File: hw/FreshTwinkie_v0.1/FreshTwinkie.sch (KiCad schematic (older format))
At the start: 50 parts, among them J1 USB_C_Receptacle, J2 USB_B_Micro, P1 USB_C_Plug, Q1 BSD840NH6327XTSA1, Q2 BSD840NH6327XTSA1, Q3 BSD840NH6327XTSA1, Q4 BSD840NH6327XTSA1, SW1 SW_Push, U1 AD8606ARMZ-REEL, U2 STM32F072CBUx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

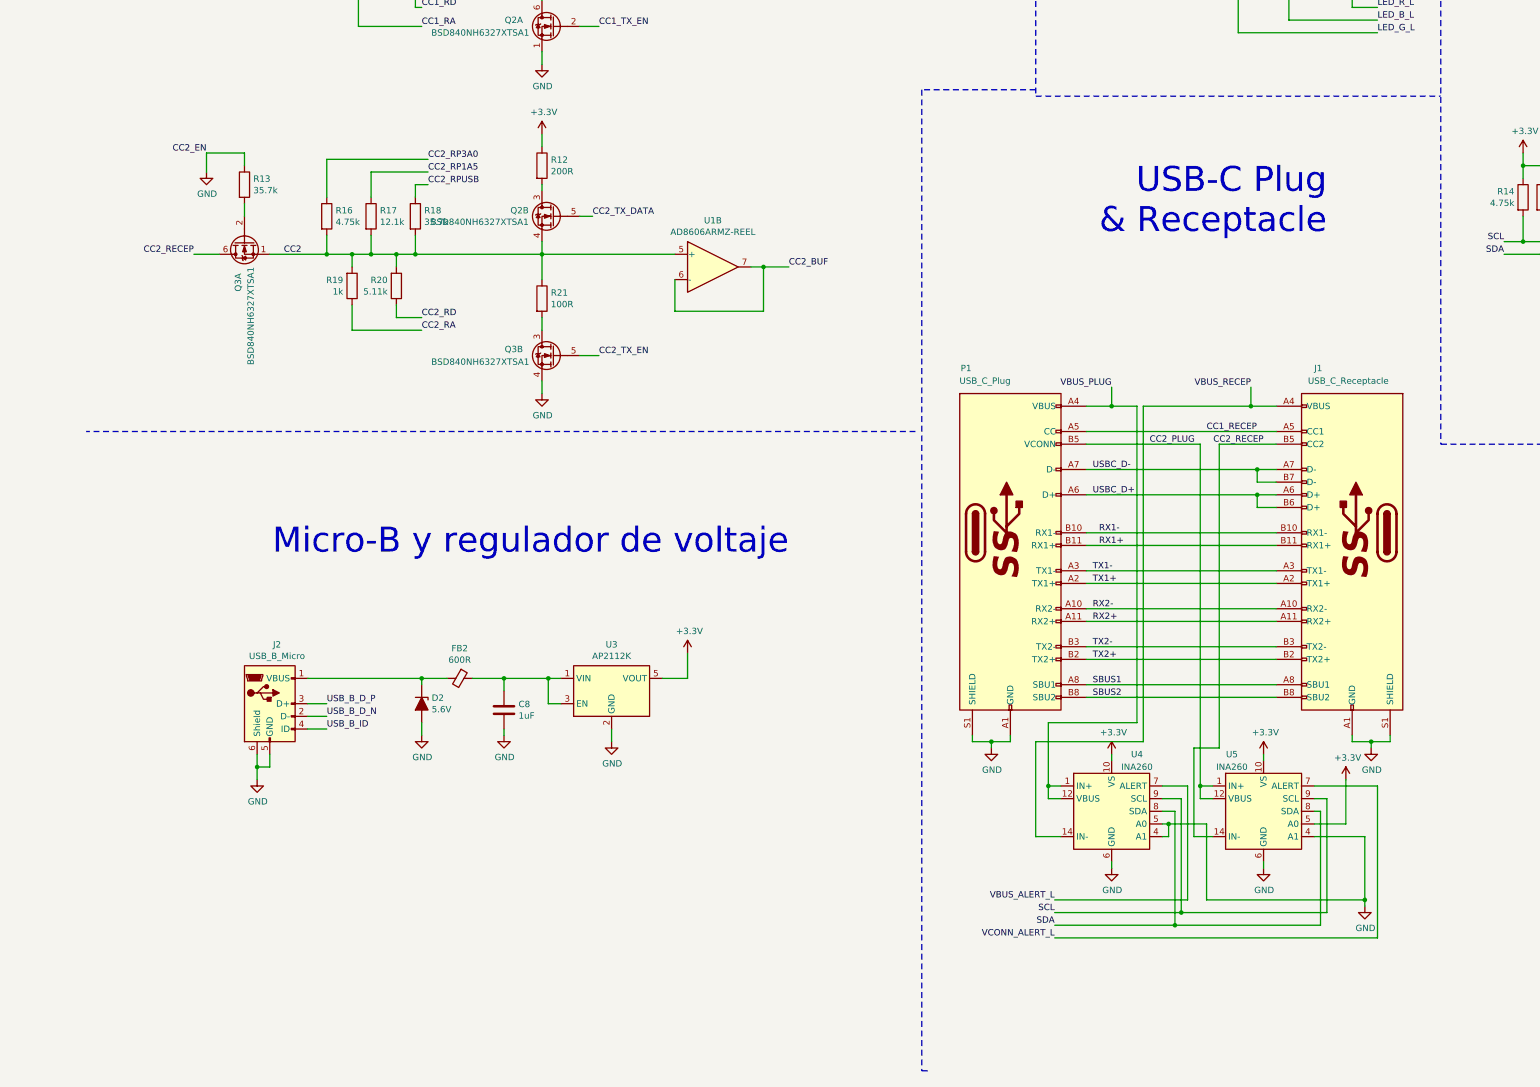
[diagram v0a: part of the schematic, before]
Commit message: switchINA260&RShunt
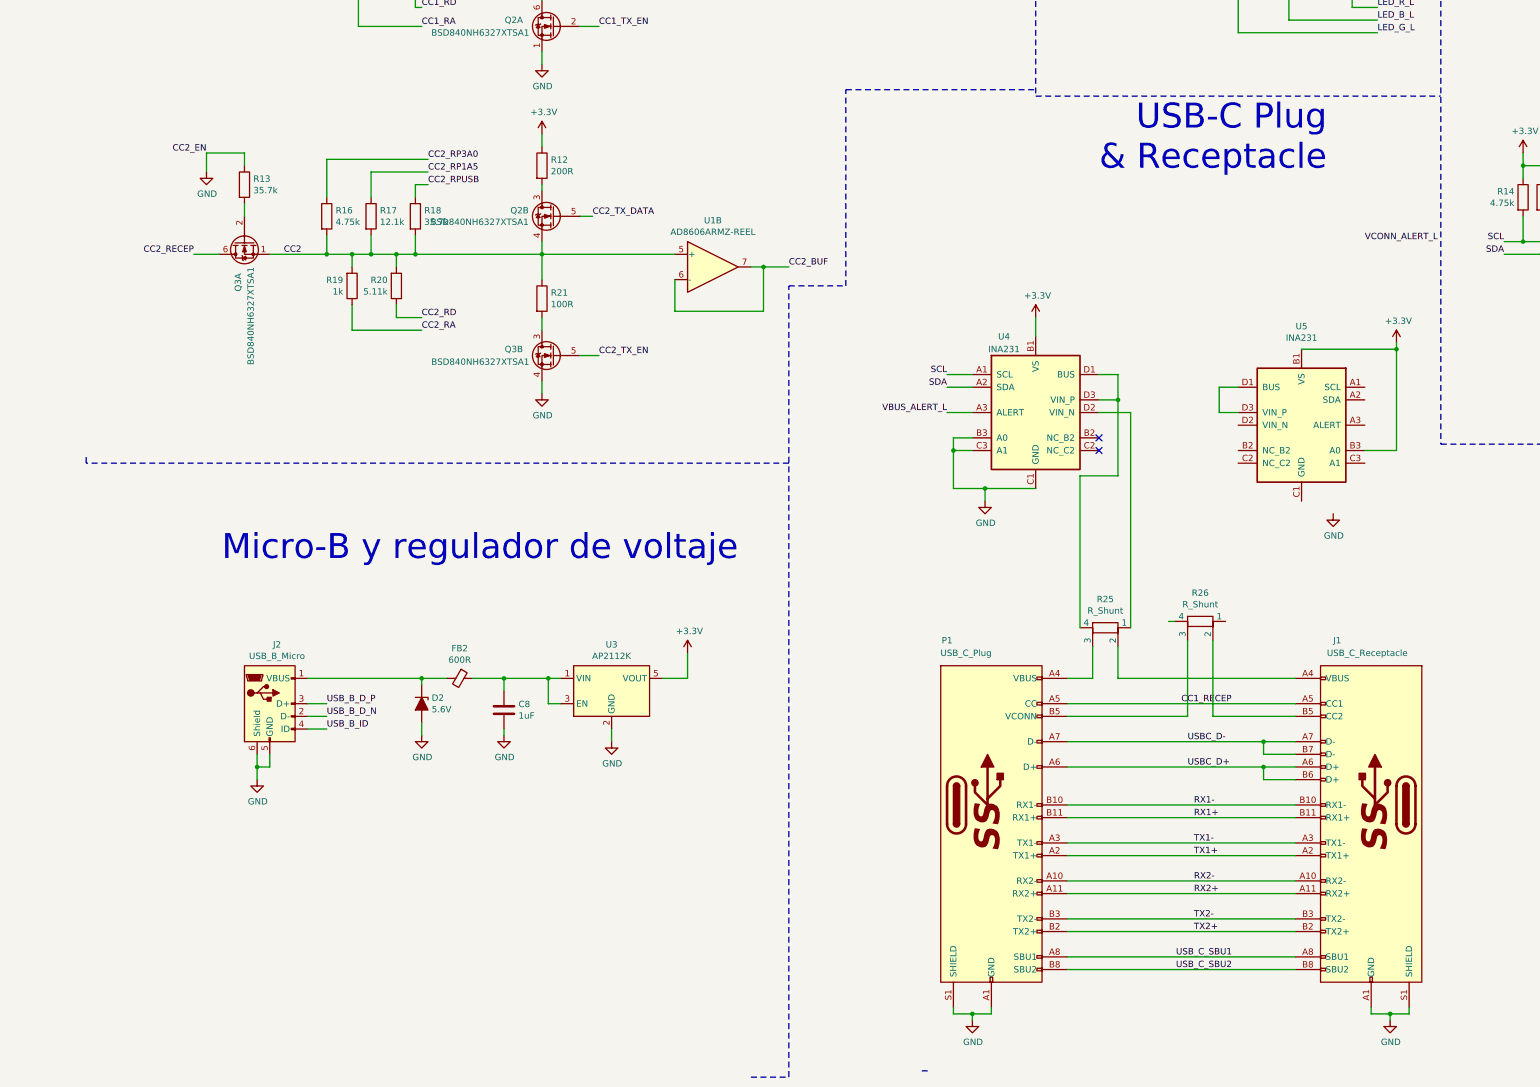
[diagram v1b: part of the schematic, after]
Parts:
- removed U4, U5: INA260, Package_SO:TSSOP-16_4.4x5mm_P0.65mm, symbol Sensor:INA260
- added R25, R26: R_Shunt, symbol Device:R_Shunt
- added U4, U5: INA231, symbol gkl_sensor:INA231
- C1: footprint Capacitor_SMD:C_0805_2012Metric -> Capacitor_SMD:C_0603_1608Metric; Mfg Taiyo Yuden -> Samsung; PN C385902 -> C1705
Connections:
- net +3V3: now also U4.B1 (VS), U5.B1 (VS), U5.B3 (A0)
- net CC2_RECEP: no longer J1.B5 (CC2)
- net GND: now also U4.B3 (A0), U4.C1 (GND), U4.C3 (A1)
- net SCL: now also U4.A1 (SCL)
- net SDA: now also U4.A2 (SDA)
- net VBUS_ALERT_L: now also U4.A3 (ALERT)
- net CC2_PLUG: no longer names the net of P1.B5 (VCONN)
- net CC2_PLUG: now also R26.3
- net SBUS1 renamed USB_C_SBU1
- net SBUS2 renamed USB_C_SBU2
- net VBUS_PLUG: no longer names the net of P1.A4 (VBUS), P1.A9 (VBUS), P1.B4 (VBUS), P1.B9 (VBUS)
- net VBUS_PLUG: now also R25.3
- net VBUS_RECEP: no longer names the net of J1.A4 (VBUS), J1.A9 (VBUS), J1.B4 (VBUS), J1.B9 (VBUS)
- net VBUS_RECEP: now also R25.2
- new net: J1.B5 (CC2), R26.2
- new net: R25.1, U4.D2 (VIN_N)
- new net: R25.4, U4.D1 (BUS), U4.D3 (VIN_P)
- new net: U5.D1 (BUS), U5.D3 (VIN_P)
- no-connect marks 6 -> 8
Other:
- moved on the sheet: J1, P1

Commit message: schChanged
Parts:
- added NT1: Net-Tie_2, NetTie:NetTie-2_SMD_Pad0.5mm, symbol Device:Net-Tie_2
- R25, R26: value R_Shunt -> 0.015R; footprint (none) -> gkl_dipol:4W_R_1206; Mfg (none) -> Vishay; PN (none) -> 71-WSK1206R0150FEA18; Tienda (none) -> Mouser
- U4, U5: footprint (none) -> BGA12N40P3X4_119X159X62N:BGA12N40P3X4_119X159X62N; Mfg (none) -> Texas Instruments; PN (none) -> 595-INA231AIYFFR; Tienda (none) -> Mouser
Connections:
- net CC2_RECEP is gone; now on net USBC_CC2: Q3.6 (D)
- net VCONN_ALERT_L is gone; now on net CC2_ALERT_L: U2.17 (PA7)
- net CC1_RA: now also U2.29 (PA8); no longer U2.45 (PB8)
- net CC1_RD: now also U2.41 (PB5); no longer U2.39 (PB3)
- net CC1_RP1A5: now also U2.37 (PA14); no longer U2.41 (PB5)
- net CC1_RP3A0: no longer U2.3 (PC14)
- net CC1_RPUSB: now also U2.34 (PA13); no longer U2.37 (PA14)
- net CC1_TX_EN: now also U2.19 (PB1); no longer U2.34 (PA13)
- net CC2_RA: now also U2.28 (PB15); no longer U2.29 (PA8)
- net CC2_RD: now also U2.45 (PB8); no longer U2.26 (PB13)
- net CC2_RP1A5: now also U2.3 (PC14); no longer U2.28 (PB15)
- net CC2_RP3A0: now also U2.4 (PC15)
- net CC2_RPUSB: now also U2.18 (PB0); no longer U2.25 (PB12)
- net CC2_TX_EN: now also U2.39 (PB3); no longer U2.2 (PC13)
- net GND: now also R13.2, R2.2, U5.C1 (GND), U5.C3 (A1); no longer R13.1, R2.1, U2.10 (PA0), U2.12 (PA2)
- net LED_G_L: now also U2.22 (PB11); no longer U2.21 (PB10)
- net LED_R_L: now also U2.26 (PB13); no longer U2.22 (PB11)
- net SCL: now also U5.A1 (SCL)
- net SDA: now also U5.A2 (SDA)
- net TX_CLKIN: now also NT1.1
- net TX_CLKOUT: now also NT1.2
- net USBC_CC2: now reaches J1.B5 (CC2), R26.2
- net CC1_EN: now reaches Q1.5 (G)
- net CC1_EN: now also R2.1, U2.10 (PA0); no longer R2.2
- net CC2_EN: now reaches Q3.2 (G)
- net CC2_EN: now also R13.1, U2.12 (PA2); no longer R13.2
- net USBC_VBUS_-: now reaches R25.1, U4.D2 (VIN_N)
- net USBC_VBUS_+: now reaches R25.4, U4.D1 (BUS), U4.D3 (VIN_P)
- net USBC_CC2_-: now reaches R26.1
- net USBC_CC2_-: now also U5.D2 (VIN_N)
- net USBC_CC2_+: now reaches R26.4
- net USBC_CC2_+: now also U5.D1 (BUS), U5.D3 (VIN_P)
- net CC2_ALERT_L: now reaches U5.A3 (ALERT)
- net CC1_RECEP renamed USBC_CC1
- net USB_B_D_N renamed USB_B_D-
- net USB_B_D_P renamed USB_B_D+
- no-connect marks 8 -> 9
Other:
- moved on the sheet: R13, R2

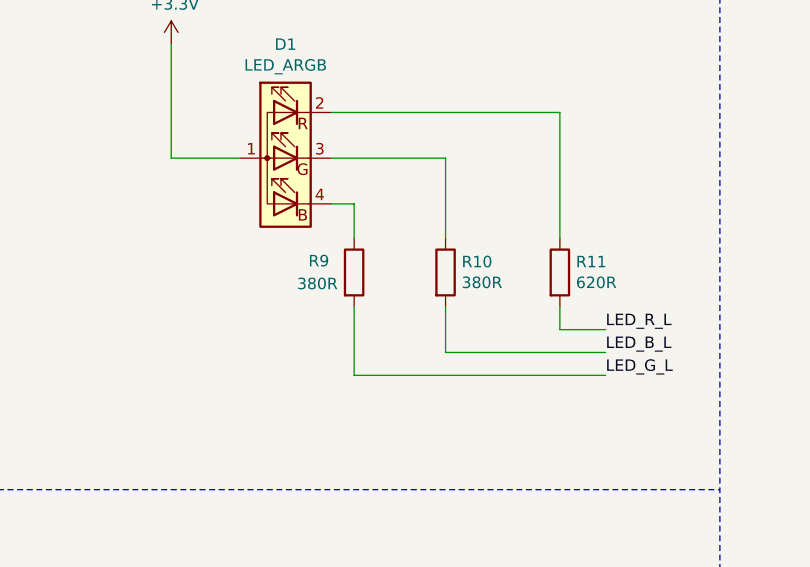
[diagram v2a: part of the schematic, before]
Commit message: 0805into0402components
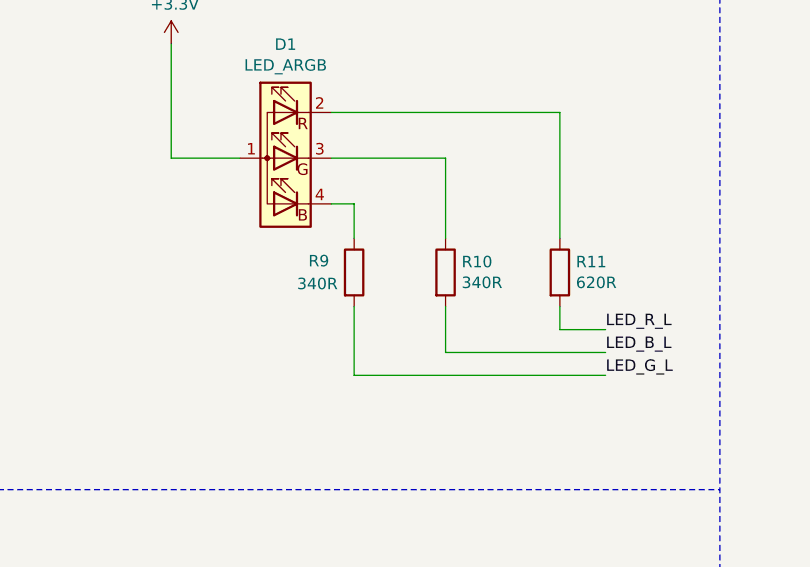
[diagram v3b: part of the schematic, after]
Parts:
- C1: footprint Capacitor_SMD:C_0603_1608Metric -> Capacitor_SMD:C_01005_0402Metric; Mfg Samsung -> Murata; PN C1705 -> C77004
- C2, C3, C7: footprint Capacitor_SMD:C_0805_2012Metric -> Capacitor_SMD:C_01005_0402Metric; Mfg Samsung -> YAGEO; PN 187-CL21F104ZAANNNC -> C60474; Tienda Mouser -> LCSC
- C4: footprint Capacitor_SMD:C_0805_2012Metric -> Capacitor_SMD:C_01005_0402Metric; PN C83170 -> C272878
- C5, C8: footprint Capacitor_SMD:C_0805_2012Metric -> Capacitor_SMD:C_01005_0402Metric; PN 187-CL21B105KOFNFNE -> C307454; Tienda Mouser -> LCSC
- C6: footprint Capacitor_SMD:C_0805_2012Metric -> Capacitor_SMD:C_01005_0402Metric; Mfg Taiyo Yuden -> Murata; PN C385902 -> C77004
- FB1, FB2: footprint Inductor_SMD:L_0805_2012Metric_Pad1.15x1.40mm_HandSolder -> Inductor_SMD:L_01005_0402Metric; PN 81-BLM21A601F -> 81-BLM15BX601SN1D
- R1, R12: footprint Resistor_SMD:R_0805_2012Metric -> Resistor_SMD:R_01005_0402Metric; Mfg PANASONIC -> TyoHM; PN C473273 -> C325381
- R10, R9: value 380R -> 340R; footprint Resistor_SMD:R_0805_2012Metric -> Resistor_SMD:R_01005_0402Metric; Mfg BOURNS -> Viking Tech; PN 652-CR0805FX-3830ELF -> C284520; Tienda Mouser -> LCSC
- R11: footprint Resistor_SMD:R_0805_2012Metric -> Resistor_SMD:R_01005_0402Metric; Mfg YAGEO -> ROHM Semicon; PN 603-RC0402FR-07620RL -> C525583; Tienda Mouser -> LCSC
- R13, R18, R2, R22, R23, R5: footprint Resistor_SMD:R_0805_2012Metric -> Resistor_SMD:R_01005_0402Metric; PN C218528 -> C284526
- R14, R15, R16, R3: footprint Resistor_SMD:R_0805_2012Metric -> Resistor_SMD:R_01005_0402Metric; Mfg UNI-ROYAL -> YAGEO; PN C425496 -> C723406
- R17, R4: footprint Resistor_SMD:R_0805_2012Metric -> Resistor_SMD:R_01005_0402Metric; Mfg Viking Tech -> YAGEO; PN C217800 -> C281773
- R19, R6: footprint Resistor_SMD:R_0805_2012Metric -> Resistor_SMD:R_01005_0402Metric; Mfg FH -> Viking Tech; PN C115302 -> C317916
- R20, R7: footprint Resistor_SMD:R_0805_2012Metric -> Resistor_SMD:R_01005_0402Metric; Mfg BOURNS -> YAGEO; PN C204553 -> C274895
- R21, R24, R8: footprint Resistor_SMD:R_0805_2012Metric -> Resistor_SMD:R_01005_0402Metric; Mfg Viking Tech -> TyoHM; PN C515718 -> C325391

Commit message: change0402into0603
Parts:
- C1, C2, C3, C4, C5, C6, C7, C8: footprint Capacitor_SMD:C_01005_0402Metric -> Capacitor_SMD:C_0603_1608Metric
- R1, R10, R11, R12, R13, R14, R15, R16, R17, R18, R19, R2, R20, R21, R22, R23, R24, R3, R4, R5, R6, R7, R8, R9: footprint Resistor_SMD:R_01005_0402Metric -> Resistor_SMD:R_0603_1608Metric

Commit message: usbmicroB&regulatorReady
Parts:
- FB1, FB2: footprint Inductor_SMD:L_01005_0402Metric -> Inductor_SMD:L_0603_1608Metric
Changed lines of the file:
@@
 F 0 "FB1" V 15063 2250 50  0000 C CNN
 F 1 "600R" V 15154 2250 50  0000 C CNN
-F 2 "Inductor_SMD:L_01005_0402Metric" V 15230 2250 50  0001 C CNN
+F 2 "Inductor_SMD:L_0603_1608Metric" V 15230 2250 50  0001 C CNN
 F 3 "https://www.mouser.mx/datasheet/2/281/ENFA0018-1915754.pdf" H 15300 2250 50  0001 C CNN
 F 4 "Murata Electronics" H 15300 2250 50  0001 C CNN "Mfg"
@@
 F 0 "FB2" V 3213 8050 50  0000 C CNN
 F 1 "600R" V 3304 8050 50  0000 C CNN
-F 2 "Inductor_SMD:L_01005_0402Metric" V 3380 8050 50  0001 C CNN
+F 2 "Inductor_SMD:L_0603_1608Metric" V 3380 8050 50  0001 C CNN
 F 3 "https://www.mouser.mx/datasheet/2/281/ENFA0018-1915754.pdf" H 3450 8050 50  0001 C CNN
 F 4 "Murata Electronics" H 3450 8050 50  0001 C CNN "Mfg"

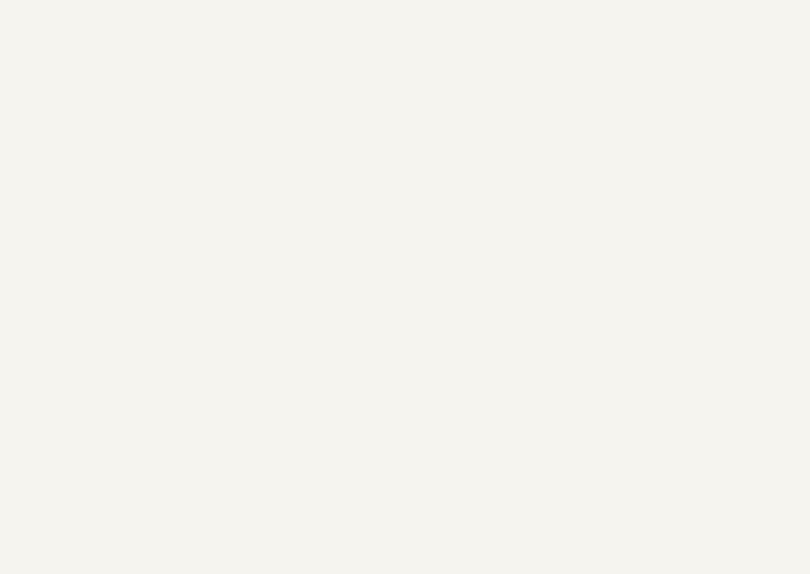
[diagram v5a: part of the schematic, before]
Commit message: components_place
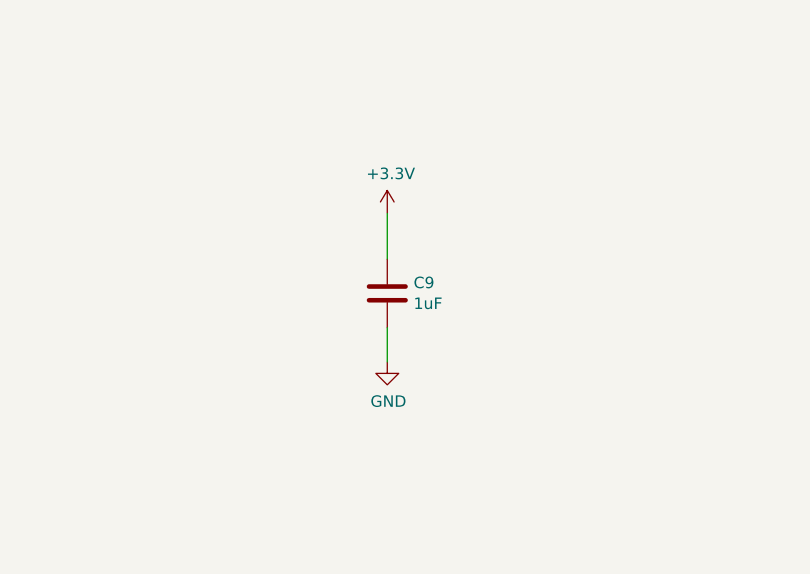
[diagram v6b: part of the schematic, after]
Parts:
- added C9: 1uF, Capacitor_SMD:C_0603_1608Metric, symbol Device:C
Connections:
- net +3V3: now also C9.1
- net GND: now also C9.2
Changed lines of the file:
@@
 Text Label 14450 5000 0    50   ~ 0
 UART_RX
+$Comp
+L Device:C C9
+U 1 1 60447FAF
+P 3700 10050
+F 0 "C9" H 3815 10096 50  0000 L CNN
+F 1 "1uF" H 3815 10005 50  0000 L CNN
+F 2 "Capacitor_SMD:C_0603_1608Metric" H 3738 9900 50  0001 C CNN
+F 3 "https://datasheet.lcsc.com/szlcsc/1811091616_Samsung-Electro-Mechanics-CL05X105KA5NQNC_C307454.pdf" H 3700 10050 50  0001 C CNN
+F 4 "Samsung" H 3700 10050 50  0001 C CNN "Mfg"
+F 5 " 	C307454" H 3700 10050 50  0001 C CNN "PN"
+F 6 "LCSC" H 3700 10050 50  0001 C CNN "Tienda"
+	1    3700 10050
+	1    0    0    -1
+$EndComp
+$Comp
+L power:GND #PWR028
+U 1 1 604485BD
+P 3700 10350
+F 0 "#PWR028" H 3700 10100 50  0001 C CNN
+F 1 "GND" H 3705 10177 50  0000 C CNN
+F 2 "" H 3700 10350 50  0001 C CNN
+F 3 "" H 3700 10350 50  0001 C CNN
+	1    3700 10350
+	1    0    0    -1
+$EndComp
+$Comp
+L power:+3.3V #PWR027
+U 1 1 6044897D
+P 3700 9700
+F 0 "#PWR027" H 3700 9550 50  0001 C CNN
+F 1 "+3.3V" H 3715 9873 50  0000 C CNN
+F 2 "" H 3700 9700 50  0001 C CNN
+F 3 "" H 3700 9700 50  0001 C CNN
+	1    3700 9700
+	1    0    0    -1
+$EndComp
+Wire Wire Line
+	3700 9900 3700 9700
+Wire Wire Line
+	3700 10200 3700 10350
 $EndSCHEMATC
